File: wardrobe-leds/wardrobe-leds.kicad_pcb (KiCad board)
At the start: 2 copper layers, 91.4 x 50.8 mm, 48 parts, among them J1 LED strip, J2 LED strip, J3 LED strip, J4 LED strip, J5 Power, Q1 IRF540N, Q2 IRF540N, Q3 IRF540N, Q4 IRF540N, U1 LM339

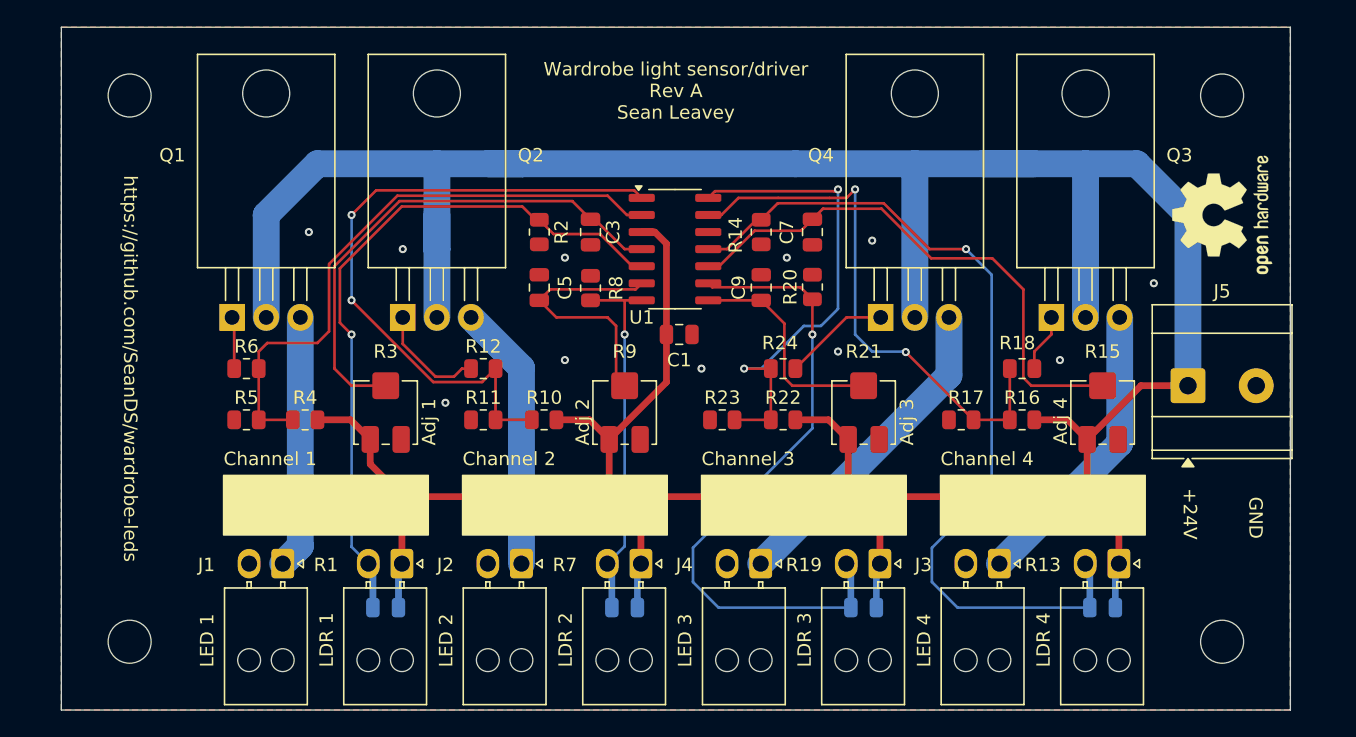
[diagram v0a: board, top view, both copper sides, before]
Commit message: Update driver to use P-channel MOSFET to avoid Vgs voltage drop; add dimmer control; add hysteresis
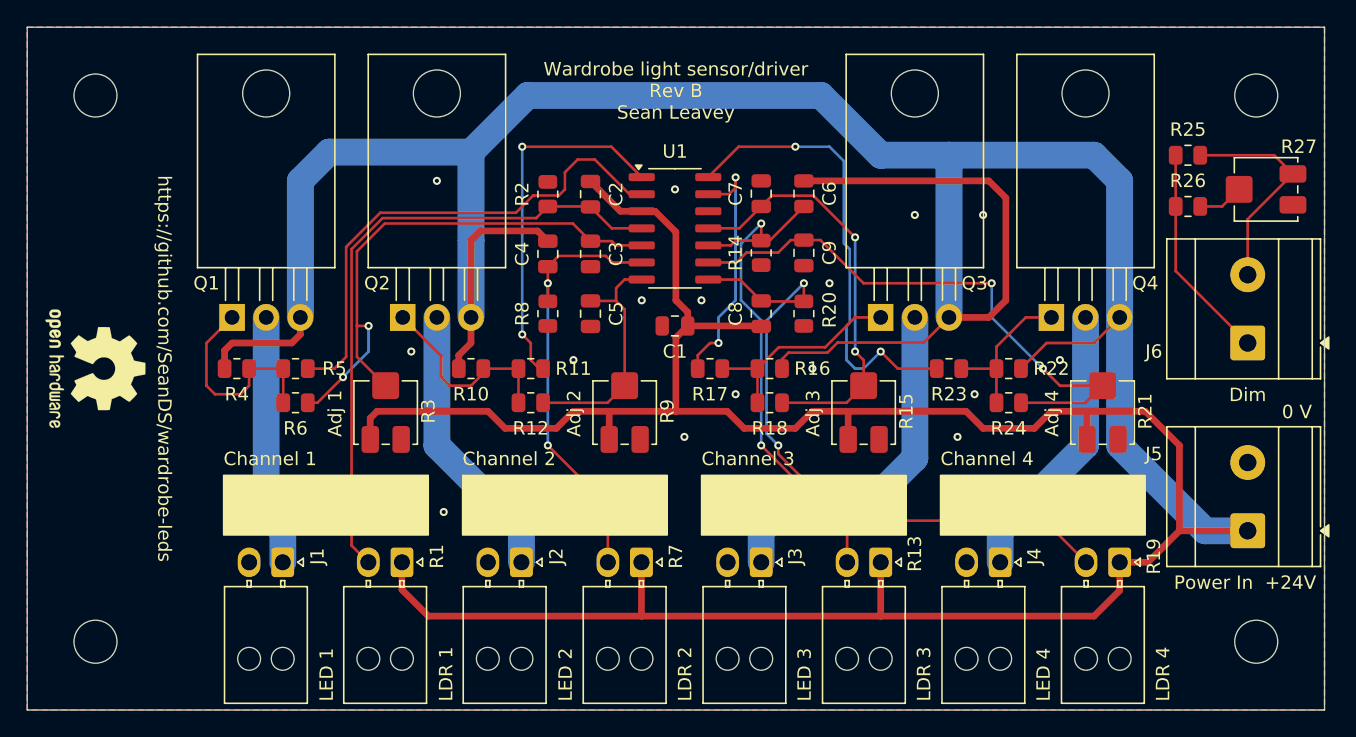
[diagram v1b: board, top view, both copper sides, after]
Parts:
- removed the R21 at (152.4, 110.0)
- removed the R22 at (146.4, 110.5)
- removed the R23 at (141.9, 110.5)
- added J6: Dim, TerminalBlock_Phoenix:TerminalBlock_Phoenix_MKDS-3-2-5.08_1x02_P5.08mm_Horizontal, F.Cu at (181.0, 104.8)
- added R12: 1M, Resistor_SMD:R_0805_2012Metric, F.Cu at (127.6, 109.2)
- added R18: 1M, Resistor_SMD:R_0805_2012Metric, F.Cu at (145.4, 109.2)
- added R25: NP, Resistor_SMD:R_0805_2012Metric, F.Cu at (176.5, 90.8)
- added R26: 0R, Resistor_SMD:R_0805_2012Metric, F.Cu at (176.5, 94.6)
- added R27: 50k, Potentiometer_SMD:Potentiometer_Bourns_3314J_Vertical, F.Cu at (182.3, 93.3)
- added R6: 1M, Resistor_SMD:R_0805_2012Metric, F.Cu at (110.1, 109.2)
- C2, C4, C6, C8: moved to F.Cu
- Q1, Q2, Q3, Q4: value IRF540N -> IRF9540N
- R10: renamed from R9; value 50k -> 10k; footprint Potentiometer_SMD:Potentiometer_Bourns_3314J_Vertical -> Resistor_SMD:R_0805_2012Metric
- R13: renamed from R11; value 100k -> NSL-19M51; footprint Resistor_SMD:R_0805_2012Metric -> Connector_Molex:Molex_Nano-Fit_105313-xx02_1x02_P2.50mm_Horizontal
- R14: renamed from R12; value 100R -> 100k
- R15: renamed from R13; value NSL-19M51 -> 50k; footprint Connector_Molex:Molex_Nano-Fit_105313-xx02_1x02_P2.50mm_Horizontal -> Potentiometer_SMD:Potentiometer_Bourns_3314J_Vertical
- R16: renamed from R14; value 100k -> 10k
- R17: renamed from R15; value 50k -> 10k; footprint Potentiometer_SMD:Potentiometer_Bourns_3314J_Vertical -> Resistor_SMD:R_0805_2012Metric
- R19: renamed from R16; value 10k -> NSL-19M51; footprint Resistor_SMD:R_0805_2012Metric -> Connector_Molex:Molex_Nano-Fit_105313-xx02_1x02_P2.50mm_Horizontal
- R21: renamed from R18; value 100R -> 50k; footprint Resistor_SMD:R_0805_2012Metric -> Potentiometer_SMD:Potentiometer_Bourns_3314J_Vertical
- R22: renamed from R19; value NSL-19M51 -> 10k; footprint Connector_Molex:Molex_Nano-Fit_105313-xx02_1x02_P2.50mm_Horizontal -> Resistor_SMD:R_0805_2012Metric
- R23: renamed from R20; value 100k -> 10k
- R24: value 100R -> 1M
- R5: value 100k -> 10k
- R7: renamed from R6; value 100R -> NSL-19M51; footprint Resistor_SMD:R_0805_2012Metric -> Connector_Molex:Molex_Nano-Fit_105313-xx02_1x02_P2.50mm_Horizontal
- R8: renamed from R7; value NSL-19M51 -> 100k; footprint Connector_Molex:Molex_Nano-Fit_105313-xx02_1x02_P2.50mm_Horizontal -> Resistor_SMD:R_0805_2012Metric
- R9: renamed from R8; value 100k -> 50k; footprint Resistor_SMD:R_0805_2012Metric -> Potentiometer_SMD:Potentiometer_Bourns_3314J_Vertical
- moved REF** 84.6 mm to (95.2, 106.7), turned to -90 degrees
- moved C6 38.0 mm to (148.0, 93.7), turned to -90 degrees
- moved C2 34.3 mm to (132.1, 93.7), turned to -90 degrees
- moved R7 32.7 mm to (135.9, 121.1), turned to -90 degrees
- moved R13 31.4 mm to (153.7, 121.1), turned to -90 degrees
- moved R17 29.4 mm to (141.0, 106.7), turned to 0 degrees
- moved C4 26.9 mm to (128.9, 98.1), turned to -90 degrees
- moved C8 23.2 mm to (144.8, 102.6), turned to 90 degrees
- moved R14 22.4 mm to (144.8, 98.1), turned to -90 degrees
- moved R15 22.1 mm to (152.4, 110.0), turned to 180 degrees
- moved R8 19.8 mm to (128.9, 102.6)
- moved J4 17.8 mm to (162.6, 121.1)
- moved J3 17.7 mm to (144.8, 121.1)
- moved R22 17.4 mm to (163.2, 106.7), turned to 0 degrees
- moved R24 17.0 mm to (163.2, 109.2)
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- renumbered R10 to R11, R17 to R20
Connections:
- C2 pad 2: Net-(U1A-+) -> Net-(U1A--)
- C3 pad 1: Net-(U1A--) -> Net-(U1A-+)
- C4 pad 2: Net-(U1B-+) -> Net-(U1B--)
- C5 pad 1: Net-(U1B--) -> Net-(U1B-+)
- C6 pad 2: Net-(U1C-+) -> Net-(U1C--)
- C7 pad 1: Net-(U1C--) -> Net-(U1C-+)
- C8 pad 2: Net-(U1D-+) -> Net-(U1D--)
- C9 pad 1: Net-(U1D--) -> Net-(U1D-+)
- Q1 pad 2: +24V -> Net-(J1-Pin_1)
- Q1 pad 3: Net-(J1-Pin_1) -> +24V
- Q2 pad 2: +24V -> Net-(J2-Pin_1)
- Q2 pad 3: Net-(J2-Pin_1) -> +24V
- Q3 pad 2: +24V -> Net-(J3-Pin_1)
- Q3 pad 3: Net-(J3-Pin_1) -> +24V
- Q4 pad 2: +24V -> Net-(J4-Pin_1)
- Q4 pad 3: Net-(J4-Pin_1) -> +24V
- R1 pad 2: Net-(U1A-+) -> Net-(U1A--)
- R10 pad 1: +24V -> Net-(Q2-G)
- R10 pad 2: Net-(U1B--) -> +24V
- R11 pad 1: Net-(R10-Pad1) -> Net-(R11-Pad1)
- R11 pad 2: +24V -> Net-(Q2-G)
- R13 pad 1: GND -> +24V
- R13 pad 2: Net-(R10-Pad1) -> Net-(U1C--)
- R14 pad 1: Net-(Q2-G) -> Net-(U1C--)
- R14 pad 2: Net-(R10-Pad1) -> GND
- R16 pad 1: Net-(U1C-+) -> Net-(Q3-G)
- R16 pad 2: GND -> +24V
- R17 pad 1: +24V -> Net-(R17-Pad1)
- R17 pad 2: Net-(U1C--) -> Net-(Q3-G)
- R19 pad 1: Net-(R16-Pad1) -> +24V
- R19 pad 2: +24V -> Net-(U1D--)
- R2 pad 1: Net-(U1A-+) -> Net-(U1A--)
- R20 pad 1: GND -> Net-(U1D--)
- R20 pad 2: Net-(R16-Pad1) -> GND
- R21 pad 1: Net-(Q3-G) -> +24V
- R21 pad 2: Net-(R16-Pad1) -> Net-(U1D-+)
- R22 pad 1: +24V -> Net-(Q4-G)
- R22 pad 2: Net-(U1D-+) -> +24V
- R23 pad 1: Net-(U1D-+) -> Net-(R23-Pad1)
- R23 pad 2: GND -> Net-(Q4-G)
- R24 pad 1: Net-(Q4-G) -> Net-(U1D-+)
- R24 pad 2: Net-(R22-Pad1) -> Net-(Q4-G)
- R3 pad 2: Net-(U1A--) -> Net-(U1A-+)
- R4 pad 1: Net-(R4-Pad1) -> Net-(Q1-G)
- R5 pad 1: GND -> Net-(Q1-G)
- R5 pad 2: Net-(R4-Pad1) -> Net-(R5-Pad2)
- R7 pad 1: Net-(Q1-G) -> +24V
- R7 pad 2: Net-(R4-Pad1) -> Net-(U1B--)
- R8 pad 1: +24V -> Net-(U1B--)
- R8 pad 2: Net-(U1B-+) -> GND
- R9 pad 1: Net-(U1B-+) -> +24V
- R9 pad 2: GND -> Net-(U1B-+)
- U1 pad 1: Net-(R10-Pad1) -> Net-(R11-Pad1)
- U1 pad 13: Net-(R16-Pad1) -> Net-(R17-Pad1)
- U1 pad 14: Net-(R22-Pad1) -> Net-(R23-Pad1)
- U1 pad 2: Net-(R4-Pad1) -> Net-(R5-Pad2)
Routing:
- net +24V: track 292.8 -> 392.8 mm
- net Net-(R10-Pad1): track 49.1 -> 0.00 mm, vias 2 -> 0
- net Net-(R4-Pad1): track 44.4 -> 0.00 mm
- net Net-(R16-Pad1): track 40.5 -> 0.00 mm, vias 2 -> 0
- net Net-(R5-Pad2): track 0.00 -> 37.9 mm
- net Net-(R22-Pad1): track 36.1 -> 0.00 mm, vias 2 -> 0
- net Net-(U1C-+): track 66.3 -> 31.1 mm, vias 1 -> 2
- net Net-(R23-Pad1): track 0.00 -> 34.6 mm, vias 0 -> 2
- net Net-(U1D--): track 16.6 -> 49.6 mm, vias 0 -> 2
- net Net-(R11-Pad1): track 0.00 -> 27.1 mm, vias 0 -> 2
- net Net-(R17-Pad1): track 0.00 -> 18.8 mm, vias 0 -> 2
- net Net-(J6-Pin_2): track 0.00 -> 16.4 mm
- net Net-(J6-Pin_1): track 0.00 -> 16.2 mm
- net Net-(U1B--): track 19.4 -> 32.7 mm, vias 0 -> 2
- net Net-(Q1-G): track 3.88 -> 15.9 mm
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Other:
- board size 91.4 x 50.8 mm -> 96.5 x 50.8 mm
- board text added: "0 V"
- board text added: "Dim"
- board text added: "Power In"
- board text removed: "GND"
